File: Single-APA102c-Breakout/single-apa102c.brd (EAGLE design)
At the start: 13.9 x 10.5 mm, 5 parts

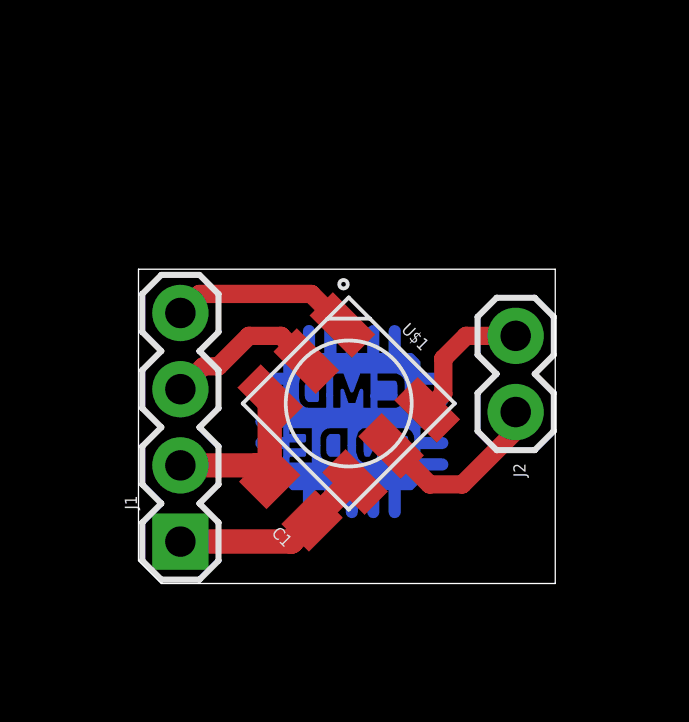
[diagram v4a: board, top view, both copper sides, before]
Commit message: adding outputs to right side
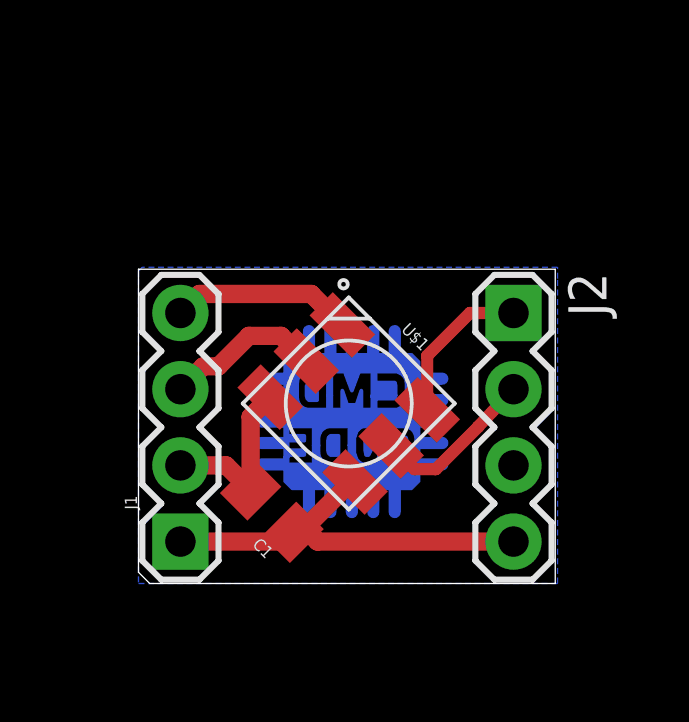
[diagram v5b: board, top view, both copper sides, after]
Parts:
- J2: device connector:1X02 -> connector:1X04
- moved J2 0.77 mm to (12.5, 9.02)
- moved C1 0.74 mm to (4.45, 2.41)
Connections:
- net GND: now also J2.3
- net VCC: now also J2.4
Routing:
- net VCC: track 6.65 -> 14.1 mm
- net DATAOUT: track 4.66 -> 5.27 mm
- net CLKOUT: track 6.05 -> 5.53 mm
- added copper zone on layer 16, net GND
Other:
- outline, holes or cut-outs redrawn
